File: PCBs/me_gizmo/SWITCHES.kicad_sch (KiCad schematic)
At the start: 11 parts, among them U1 ADG714, U2 ADG714, U3 ADG714, U4 ADG714

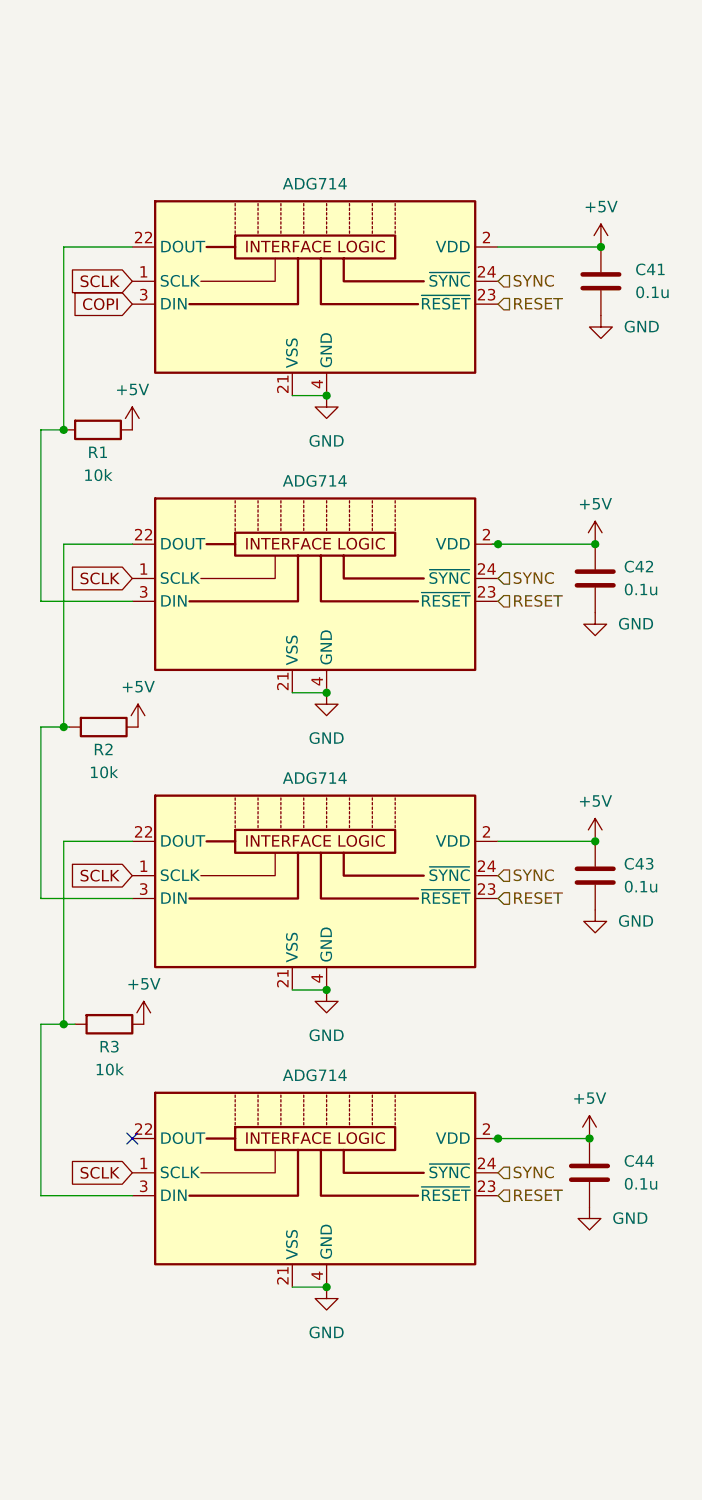
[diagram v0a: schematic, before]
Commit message: Completed first draft of integrated measurement unit
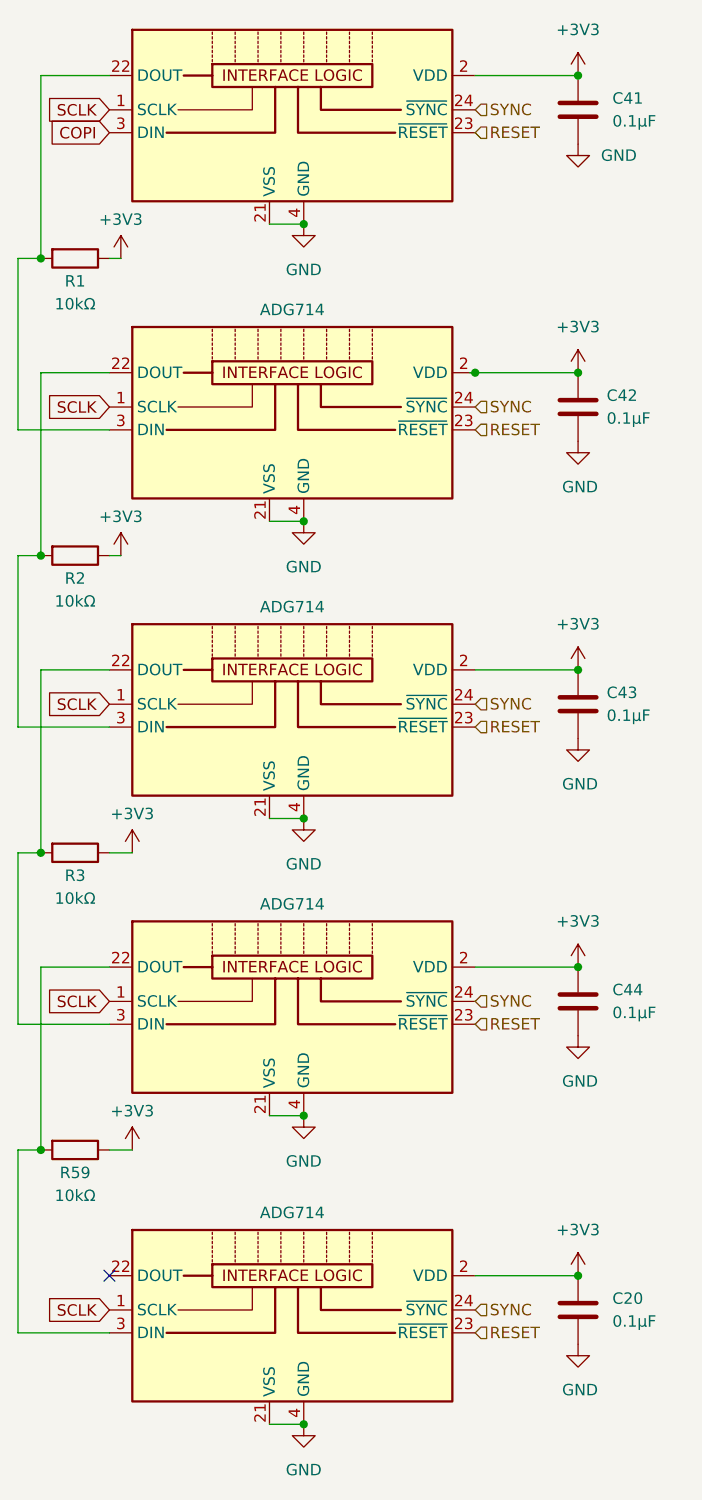
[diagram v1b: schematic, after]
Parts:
- added C20: 0.1µF, Capacitor_SMD:C_0603_1608Metric, symbol Device:C
- added R59: 10kΩ, Resistor_SMD:R_0603_1608Metric, symbol Device:R
- added U7: ADG714, Package_SO:TSSOP-24_4.4x7.8mm_P0.65mm, symbol Analog_Switch:ADG714
- C41, C42, C43, C44: value 0.1u -> 0.1µF
- R1, R2, R3: value 10k -> 10kΩ; footprint Resistor_SMD:R_0402_1005Metric_Pad0.72x0.64mm_HandSolder -> Resistor_SMD:R_0603_1608Metric
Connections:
- net COPI: now also U7.3 (DIN); no longer U1.3 (DIN)
- net GND: now also C20.2, U7.21 (VSS), U7.4 (GND)
- net RESET: now also U7.23 (~{RESET})
- net SCLK: now also U7.1 (SCLK)
- net SYNC: now also U7.24 (~{SYNC})
- net at U4.22 (DOUT): now also R3.2, U3.3 (DIN)
- net +5V renamed +3V3
- net +3V3: now also C20.1, R59.1, U7.2 (VDD)
- new net: R1.2, U1.3 (DIN), U7.22 (DOUT)
- new net: R59.2, U2.3 (DIN), U3.22 (DOUT)
- new net: R2.2, U1.22 (DOUT), U4.3 (DIN)
- now unconnected: U2.22 (DOUT)
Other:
- moved on the sheet: C41, C42, C43, C44, R1, R2, R3
